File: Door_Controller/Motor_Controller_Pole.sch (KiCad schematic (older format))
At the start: 8 parts

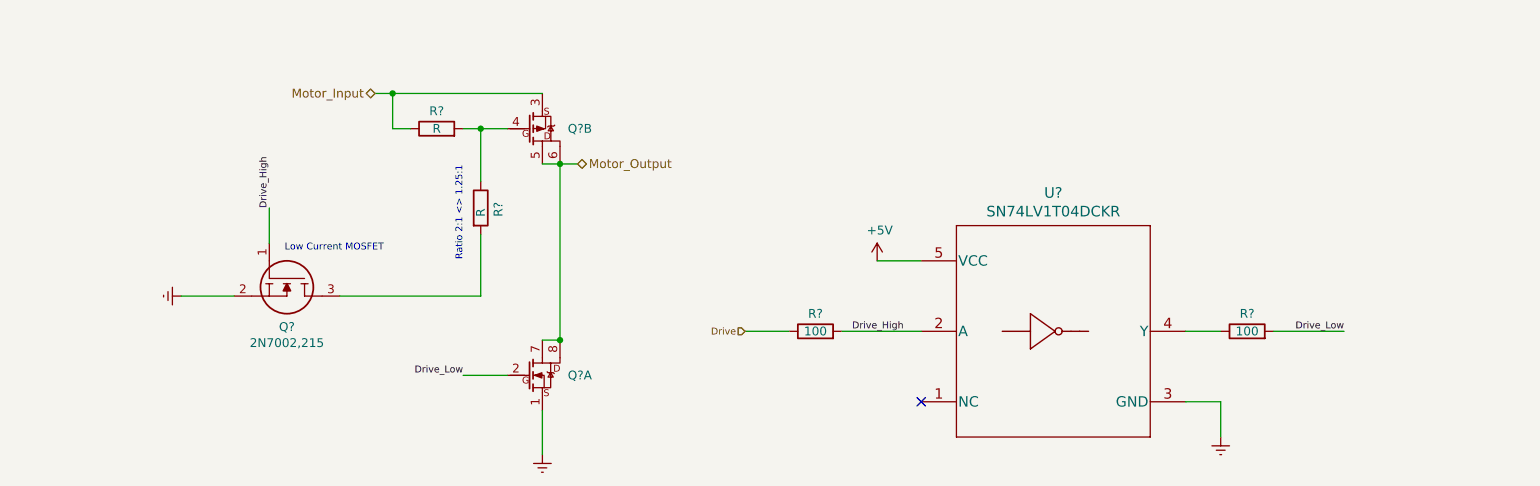
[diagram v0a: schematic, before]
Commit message: add filter caps to motor drive
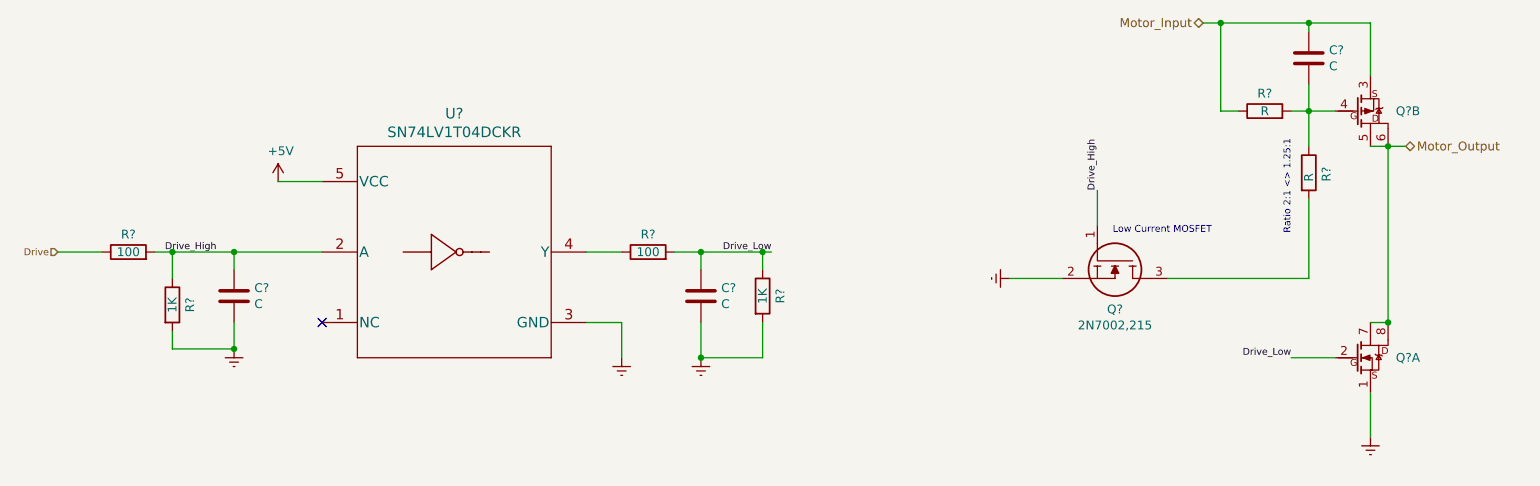
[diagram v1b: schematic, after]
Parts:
- added C? (x3): C, symbol Device:C
- added R? (x2): 1K, symbol Device:R
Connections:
- net Drive_High: now also C?.1, R?.1
- net Drive_Low: now also C?.1, R?.1
- net Earth: now also C?.2, C?.2, R?.2, R?.2
- net Motor_Input: now also C?.1
- net at Q?.4, R?.1, R?.2: now also C?.2
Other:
- moved on the sheet: Q?, Q?A, Q?B, R?, U?
